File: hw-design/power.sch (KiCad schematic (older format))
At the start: 15 parts, among them CN1 CONN_02X02, CN2 CONN_02X02

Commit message: ERC passing
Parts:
- gave numbers to parts that had none: 2
- renumbered C7 to C5, C8 to C6, RT2 to RT1, RT1 to RT2
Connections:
- wire segments 42 -> 39
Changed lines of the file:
@@
 $EndDescr
 $Comp
-L CP1 C7
+L CP1 C5
 U 1 1 548B65E4
 P 7100 2300
-F 0 "C7" V 7200 2400 50  0000 L CNN
+F 0 "C5" V 7200 2400 50  0000 L CNN
 F 1 "100uF" V 6950 2200 50  0000 L CNN
 F 2 "MOD_Footprints_Lib:CAP_RAD_5MM" H 7100 2300 60  0001 C CNN
@@
 $EndComp
 $Comp
-L C C8
+L C C6
 U 1 1 548B660A
 P 7450 2300
-F 0 "C8" V 7400 2400 40  0000 L CNN
+F 0 "C6" V 7400 2400 40  0000 L CNN
 F 1 "100nF X7R" V 7600 2150 40  0000 L CNN
 F 2 "MOD_Footprints_Lib:SM0603" H 7488 2150 30  0001 C CNN
 F 3 "~" H 7450 2300 60  0000 C CNN
 	1    7450 2300
-	1    0    0    -1
-$EndComp
-$Comp
-L PWR_FLAG #FLG06
-U 1 1 548B661E
-P 7900 1900
-F 0 "#FLG06" H 7900 1995 30  0001 C CNN
-F 1 "PWR_FLAG" H 7900 2080 30  0000 C CNN
-F 2 "" H 7900 1900 60  0000 C CNN
-F 3 "" H 7900 1900 60  0000 C CNN
-	1    7900 1900
 	1    0    0    -1
 $EndComp
@@
 $EndComp
 $Comp
-L FUSE RT1
+L FUSE RT2
 U 1 1 548B6658
 P 3550 2000
-F 0 "RT1" H 3550 2100 40  0000 C CNN
+F 0 "RT2" H 3550 2100 40  0000 C CNN
 F 1 "PTC_FUSE" H 3550 1900 40  0000 C CNN
 F 2 "MOD_Footprints_Lib:SM1210" H 3550 2000 60  0001 C CNN
@@
 $EndComp
 $Comp
-L PWR_FLAG #FLG012
+L PWR_FLAG #FLG01
 U 1 1 548B666C
 P 4350 1900
-F 0 "#FLG012" H 4350 1995 30  0001 C CNN
+F 0 "#FLG01" H 4350 1995 30  0001 C CNN
 F 1 "PWR_FLAG" H 4350 2080 30  0000 C CNN
 F 2 "" H 4350 1900 60  0000 C CNN
@@
 $EndComp
 $Comp
-L PWR_FLAG #FLG015
-U 1 1 548B66C1
-P 5900 1450
-F 0 "#FLG015" H 5900 1545 30  0001 C CNN
-F 1 "PWR_FLAG" H 5900 1630 30  0000 C CNN
-F 2 "" H 5900 1450 60  0000 C CNN
-F 3 "" H 5900 1450 60  0000 C CNN
-	1    5900 1450
-	1    0    0    -1
-$EndComp
-$Comp
-L FUSE RT2
+L FUSE RT1
 U 1 1 548B66CA
 P 3550 1650
-F 0 "RT2" H 3550 1750 40  0000 C CNN
+F 0 "RT1" H 3550 1750 40  0000 C CNN
 F 1 "PTC_FUSE" H 3550 1550 40  0000 C CNN
 F 2 "MOD_Footprints_Lib:SM2920" H 3550 1650 60  0001 C CNN
@@
 $EndComp
 $Comp
-L PWR_FLAG #FLG016
+L PWR_FLAG #FLG02
 U 1 1 54B500E8
 P 3650 2450
-F 0 "#FLG016" H 3650 2545 30  0001 C CNN
+F 0 "#FLG02" H 3650 2545 30  0001 C CNN
 F 1 "PWR_FLAG" H 3650 2630 30  0000 C CNN
 F 2 "" H 3650 2450 60  0000 C CNN
@@
 $EndComp
 $Comp
-L PWR_FLAG #FLG018
+L PWR_FLAG #FLG03
 U 1 1 54B50E4C
 P 2250 1900
-F 0 "#FLG018" H 2250 1995 30  0001 C CNN
+F 0 "#FLG03" H 2250 1995 30  0001 C CNN
 F 1 "PWR_FLAG" H 2250 2080 30  0000 C CNN
 F 2 "" H 2250 1900 60  0000 C CNN
@@
 $EndComp
 $Comp
-L AP1117E50 U?
+L AP1117E50 U1
 U 1 1 54E78C99
 P 4900 2000
-F 0 "U?" H 5000 1750 50  0000 C CNN
+F 0 "U1" H 5000 1750 50  0000 C CNN
 F 1 "AP1117E50" H 4900 2250 50  0000 C CNN
 F 2 "" H 4900 2000 60  0000 C CNN
@@
 	7100 2600 7100 2500
 Wire Wire Line
-	6900 2000 7900 2000
-Wire Wire Line
 	7100 2000 7100 2100
 Wire Wire Line
@@
 Connection ~ 7450 2000
 Wire Wire Line
-	7700 1850 7700 2000
-Wire Wire Line
-	7900 2000 7900 1900
-Connection ~ 7700 2000
+	7700 2000 7700 1850
 Wire Wire Line
 	5900 2500 5900 2600
@@
 Connection ~ 5900 2000
 Wire Wire Line
-	5550 1400 5550 2100
+	5550 1800 5550 2100
 Wire Wire Line
 	2250 2000 2650 2000
-Wire Wire Line
-	5550 1500 5900 1500
-Connection ~ 5550 1500
 Wire Wire Line
 	3900 1650 3900 2000
@@
 Connection ~ 2750 3650
 $Comp
-L AP1117E33 U?
+L AP1117E33 U2
 U 1 1 54E7BA36
 P 6600 2000
-F 0 "U?" H 6700 1750 50  0000 C CNN
+F 0 "U2" H 6700 1750 50  0000 C CNN
 F 1 "AP1117E33" H 6600 2250 50  0000 C CNN
 F 2 "" H 6600 2000 60  0000 C CNN
@@
 $EndComp
 $Comp
-L VDD #PWR?
+L VDD #PWR04
 U 1 1 54E7D8DE
 P 2550 1900
-F 0 "#PWR?" H 2550 1750 60  0001 C CNN
+F 0 "#PWR04" H 2550 1750 60  0001 C CNN
 F 1 "VDD" H 2550 2050 60  0000 C CNN
 F 2 "" H 2550 1900 60  0000 C CNN
@@
 	2550 1900 2550 2000
 $Comp
-L GNDD #PWR?
+L GNDD #PWR05
 U 1 1 54E7EDE1
 P 3650 2600
-F 0 "#PWR?" H 3650 2350 60  0001 C CNN
+F 0 "#PWR05" H 3650 2350 60  0001 C CNN
 F 1 "GNDD" H 3650 2450 60  0000 C CNN
 F 2 "" H 3650 2600 60  0000 C CNN
@@
 $EndComp
 $Comp
-L GNDD #PWR?
+L GNDD #PWR06
 U 1 1 54E7EE6C
 P 4050 2600
-F 0 "#PWR?" H 4050 2350 60  0001 C CNN
+F 0 "#PWR06" H 4050 2350 60  0001 C CNN
 F 1 "GNDD" H 4050 2450 60  0000 C CNN
 F 2 "" H 4050 2600 60  0000 C CNN
@@
 $EndComp
 $Comp
-L GNDD #PWR?
+L GNDD #PWR07
 U 1 1 54E7EE80
 P 4350 2600
-F 0 "#PWR?" H 4350 2350 60  0001 C CNN
+F 0 "#PWR07" H 4350 2350 60  0001 C CNN
 F 1 "GNDD" H 4350 2450 60  0000 C CNN
 F 2 "" H 4350 2600 60  0000 C CNN
@@
 $EndComp
 $Comp
-L GNDD #PWR?
+L GNDD #PWR08
 U 1 1 54E7F5B7
 P 1500 3750
-F 0 "#PWR?" H 1500 3500 60  0001 C CNN
+F 0 "#PWR08" H 1500 3500 60  0001 C CNN
 F 1 "GNDD" H 1500 3600 60  0000 C CNN
 F 2 "" H 1500 3750 60  0000 C CNN
@@
 $EndComp
 $Comp
-L GNDD #PWR?
+L GNDD #PWR09
 U 1 1 54E7F5CB
 P 2400 3750
-F 0 "#PWR?" H 2400 3500 60  0001 C CNN
+F 0 "#PWR09" H 2400 3500 60  0001 C CNN
 F 1 "GNDD" H 2400 3600 60  0000 C CNN
 F 2 "" H 2400 3750 60  0000 C CNN
@@
 $EndComp
 $Comp
-L GNDD #PWR?
+L GNDD #PWR010
 U 1 1 54E7F5DF
 P 2750 3750
-F 0 "#PWR?" H 2750 3500 60  0001 C CNN
+F 0 "#PWR010" H 2750 3500 60  0001 C CNN
 F 1 "GNDD" H 2750 3600 60  0000 C CNN
 F 2 "" H 2750 3750 60  0000 C CNN
@@
 $EndComp
 $Comp
-L GNDD #PWR?
+L GNDD #PWR011
 U 1 1 54E7F5F3
 P 3650 3750
-F 0 "#PWR?" H 3650 3500 60  0001 C CNN
+F 0 "#PWR011" H 3650 3500 60  0001 C CNN
 F 1 "GNDD" H 3650 3600 60  0000 C CNN
 F 2 "" H 3650 3750 60  0000 C CNN
@@
 $EndComp
 $Comp
-L GNDD #PWR?
+L GNDD #PWR012
 U 1 1 54E7F9F2
 P 5550 2600
-F 0 "#PWR?" H 5550 2350 60  0001 C CNN
+F 0 "#PWR012" H 5550 2350 60  0001 C CNN
 F 1 "GNDD" H 5550 2450 60  0000 C CNN
 F 2 "" H 5550 2600 60  0000 C CNN
@@
 $EndComp
 $Comp
-L GNDD #PWR?
+L GNDD #PWR013
 U 1 1 54E7FA28
 P 5900 2600
-F 0 "#PWR?" H 5900 2350 60  0001 C CNN
+F 0 "#PWR013" H 5900 2350 60  0001 C CNN
 F 1 "GNDD" H 5900 2450 60  0000 C CNN
 F 2 "" H 5900 2600 60  0000 C CNN
@@
 $EndComp
 $Comp
-L GNDD #PWR?
+L GNDD #PWR014
 U 1 1 54E7FA3C
 P 7100 2600
-F 0 "#PWR?" H 7100 2350 60  0001 C CNN
+F 0 "#PWR014" H 7100 2350 60  0001 C CNN
 F 1 "GNDD" H 7100 2450 60  0000 C CNN
 F 2 "" H 7100 2600 60  0000 C CNN
@@
 $EndComp
 $Comp
-L GNDD #PWR?
+L GNDD #PWR015
 U 1 1 54E7FA50
 P 7450 2600
-F 0 "#PWR?" H 7450 2350 60  0001 C CNN
+F 0 "#PWR015" H 7450 2350 60  0001 C CNN
 F 1 "GNDD" H 7450 2450 60  0000 C CNN
 F 2 "" H 7450 2600 60  0000 C CNN
@@
 $EndComp
 $Comp
-L GNDD #PWR?
+L GNDD #PWR016
 U 1 1 54E80258
 P 4900 2350
-F 0 "#PWR?" H 4900 2100 60  0001 C CNN
+F 0 "#PWR016" H 4900 2100 60  0001 C CNN
 F 1 "GNDD" H 4900 2200 60  0000 C CNN
 F 2 "" H 4900 2350 60  0000 C CNN
@@
 	4900 2300 4900 2350
 $Comp
-L +5V #PWR?
+L +5V #PWR017
 U 1 1 54E80C28
-P 5550 1400
-F 0 "#PWR?" H 5550 1250 60  0001 C CNN
-F 1 "+5V" H 5550 1540 60  0000 C CNN
-F 2 "" H 5550 1400 60  0000 C CNN
-F 3 "" H 5550 1400 60  0000 C CNN
-	1    5550 1400
-	1    0    0    -1
-$EndComp
-Wire Wire Line
-	5900 1500 5900 1450
+P 5550 1800
+F 0 "#PWR017" H 5550 1650 60  0001 C CNN
+F 1 "+5V" H 5550 1940 60  0000 C CNN
+F 2 "" H 5550 1800 60  0000 C CNN
+F 3 "" H 5550 1800 60  0000 C CNN
+	1    5550 1800
+	1    0    0    -1
+$EndComp
 Wire Wire Line
 	3200 1650 3300 1650
@@
 	3800 1650 3900 1650
 $Comp
-L +3.3VP #PWR?
+L +3.3VP #PWR018
 U 1 1 54E84DA1
 P 7700 1850
-F 0 "#PWR?" H 7750 1880 20  0001 C CNN
+F 0 "#PWR018" H 7750 1880 20  0001 C CNN
 F 1 "+3.3VP" H 7700 1940 30  0000 C CNN
 F 2 "" H 7700 1850 60  0000 C CNN
@@
 	5200 2000 6300 2000
 $Comp
-L GNDD #PWR?
+L GNDD #PWR019
 U 1 1 54E876DB
 P 6600 2350
-F 0 "#PWR?" H 6600 2100 60  0001 C CNN
+F 0 "#PWR019" H 6600 2100 60  0001 C CNN
 F 1 "GNDD" H 6600 2200 60  0000 C CNN
 F 2 "" H 6600 2350 60  0000 C CNN
@@
 	6600 2300 6600 2350
 $Comp
-L +9V #PWR?
+L +9V #PWR020
 U 1 1 54E893A4
 P 4050 1850
-F 0 "#PWR?" H 4050 1700 60  0001 C CNN
+F 0 "#PWR020" H 4050 1700 60  0001 C CNN
 F 1 "+9V" H 4050 1990 60  0000 C CNN
 F 2 "" H 4050 1850 60  0000 C CNN
@@
 $EndComp
 Wire Wire Line
-	4600 2000 3800 2000
+	3800 2000 4600 2000
+Wire Wire Line
+	6900 2000 7700 2000
 $EndSCHEMATC

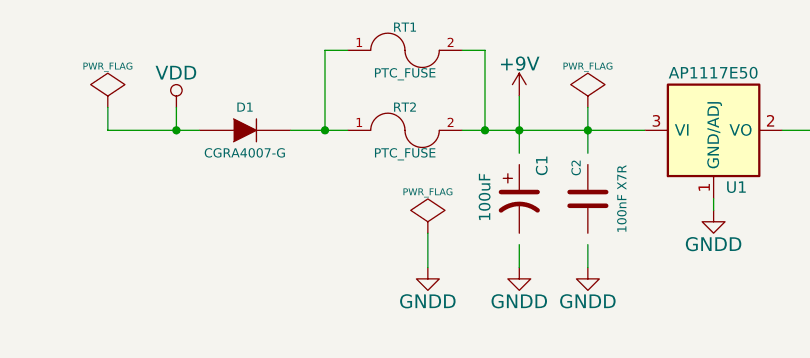
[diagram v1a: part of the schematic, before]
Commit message: removing one of the fuses
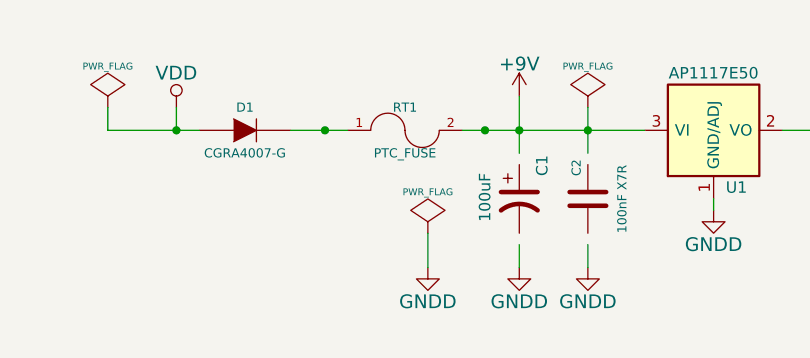
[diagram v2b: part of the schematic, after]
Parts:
- removed RT1: PTC_FUSE, MOD_Footprints_Lib:SM2920, symbol FUSE
- renumbered RT2 to RT1
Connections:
- wire segments 39 -> 35
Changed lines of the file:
@@
 $EndComp
 $Comp
-L FUSE RT2
+L FUSE RT1
 U 1 1 548B6658
 P 3550 2000
-F 0 "RT2" H 3550 2100 40  0000 C CNN
+F 0 "RT1" H 3550 2100 40  0000 C CNN
 F 1 "PTC_FUSE" H 3550 1900 40  0000 C CNN
 F 2 "MOD_Footprints_Lib:SM1210" H 3550 2000 60  0001 C CNN
@@
 $EndComp
 $Comp
-L FUSE RT1
-U 1 1 548B66CA
-P 3550 1650
-F 0 "RT1" H 3550 1750 40  0000 C CNN
-F 1 "PTC_FUSE" H 3550 1550 40  0000 C CNN
-F 2 "MOD_Footprints_Lib:SM2920" H 3550 1650 60  0001 C CNN
-F 3 "~" H 3550 1650 60  0000 C CNN
-	1    3550 1650
-	1    0    0    -1
-$EndComp
-$Comp
 L PWR_FLAG #FLG02
 U 1 1 54B500E8
@@
 Wire Wire Line
 	2250 2000 2650 2000
-Wire Wire Line
-	3900 1650 3900 2000
 Connection ~ 3900 2000
-Wire Wire Line
-	3200 1650 3200 2000
 Connection ~ 3200 2000
 Wire Wire Line
@@
 	1    0    0    -1
 $EndComp
-Wire Wire Line
-	3200 1650 3300 1650
-Wire Wire Line
-	3800 1650 3900 1650
 $Comp
 L +3.3VP #PWR018

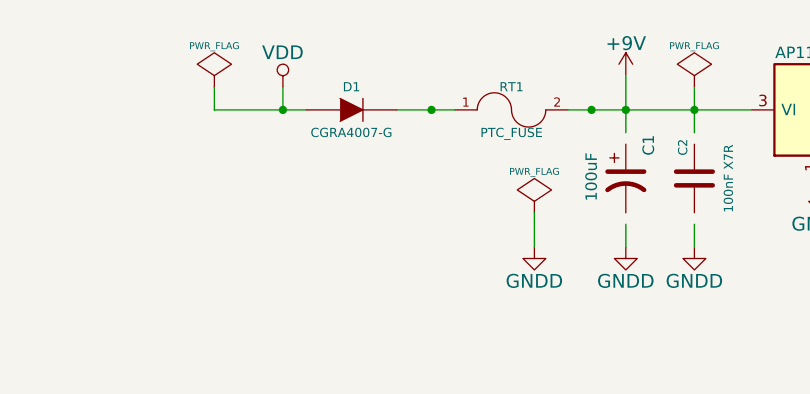
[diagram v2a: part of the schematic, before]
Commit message: wip: footprint association using default kicad libraries
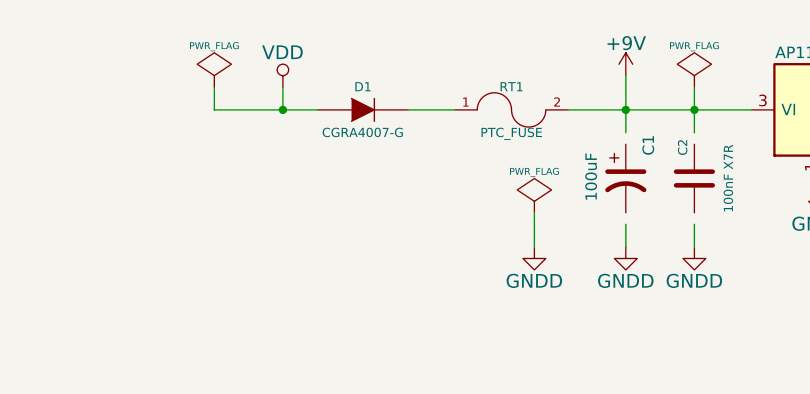
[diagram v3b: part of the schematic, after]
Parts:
- C1, C3, C5: footprint MOD_Footprints_Lib:CAP_RAD_5MM -> Capacitors_ThroughHole:Capacitor5x6RM2.5
- C2, C4, C6: footprint MOD_Footprints_Lib:SM0603 -> Capacitors_SMD:C_0603
- CN1, CN2: footprint (none) -> MOD_Footprints:CONN_PANNEL
- D1: footprint MOD_Footprints_Lib:DO-214AC(SMA) -> Diodes_SMD:Diode-SMA_Standard
- RT1: footprint MOD_Footprints_Lib:SM1210 -> Resistors_SMD:R_1210
- TP1, TP2: footprint (none) -> Pin_Headers:Pin_Header_Straight_1x01
- U1, U2: footprint (none) -> SMD_Packages:SOT-223
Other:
- moved on the sheet: D1
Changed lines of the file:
@@
 F 0 "C5" V 7200 2400 50  0000 L CNN
 F 1 "100uF" V 6950 2200 50  0000 L CNN
-F 2 "MOD_Footprints_Lib:CAP_RAD_5MM" H 7100 2300 60  0001 C CNN
+F 2 "Capacitors_ThroughHole:Capacitor5x6RM2.5" H 7100 2300 60  0001 C CNN
 F 3 "~" H 7100 2300 60  0000 C CNN
 	1    7100 2300
@@
 F 0 "C3" V 5650 2400 50  0000 L CNN
 F 1 "100uF" V 5400 2200 50  0000 L CNN
-F 2 "MOD_Footprints_Lib:CAP_RAD_5MM" H 5550 2300 60  0001 C CNN
+F 2 "Capacitors_ThroughHole:Capacitor5x6RM2.5" H 5550 2300 60  0001 C CNN
 F 3 "~" H 5550 2300 60  0000 C CNN
 	1    5550 2300
@@
 F 0 "C6" V 7400 2400 40  0000 L CNN
 F 1 "100nF X7R" V 7600 2150 40  0000 L CNN
-F 2 "MOD_Footprints_Lib:SM0603" H 7488 2150 30  0001 C CNN
+F 2 "Capacitors_SMD:C_0603" H 7488 2150 30  0001 C CNN
 F 3 "~" H 7450 2300 60  0000 C CNN
 	1    7450 2300
@@
 F 0 "C4" V 5850 2400 40  0000 L CNN
 F 1 "100nF X7R" V 6050 2150 40  0000 L CNN
-F 2 "MOD_Footprints_Lib:SM0603" H 5938 2150 30  0001 C CNN
+F 2 "Capacitors_SMD:C_0603" H 5938 2150 30  0001 C CNN
 F 3 "~" H 5900 2300 60  0000 C CNN
 	1    5900 2300
@@
 F 0 "C1" V 4150 2400 50  0000 L CNN
 F 1 "100uF" V 3900 2200 50  0000 L CNN
-F 2 "MOD_Footprints_Lib:CAP_RAD_5MM" H 4050 2300 60  0001 C CNN
+F 2 "Capacitors_ThroughHole:Capacitor5x6RM2.5" H 4050 2300 60  0001 C CNN
 F 3 "~" H 4050 2300 60  0000 C CNN
 	1    4050 2300
@@
 L DIODE D1
 U 1 1 548B6651
-P 2850 2000
-F 0 "D1" H 2850 2100 40  0000 C CNN
-F 1 "CGRA4007-G" H 2850 1900 40  0000 C CNN
-F 2 "MOD_Footprints_Lib:DO-214AC(SMA)" H 2850 2000 60  0001 C CNN
-F 3 "~" H 2850 2000 60  0000 C CNN
-	1    2850 2000
+P 2900 2000
+F 0 "D1" H 2900 2100 40  0000 C CNN
+F 1 "CGRA4007-G" H 2900 1900 40  0000 C CNN
+F 2 "Diodes_SMD:Diode-SMA_Standard" H 2900 2000 60  0001 C CNN
+F 3 "~" H 2900 2000 60  0000 C CNN
+	1    2900 2000
 	1    0    0    -1
 $EndComp
@@
 F 0 "RT1" H 3550 2100 40  0000 C CNN
 F 1 "PTC_FUSE" H 3550 1900 40  0000 C CNN
-F 2 "MOD_Footprints_Lib:SM1210" H 3550 2000 60  0001 C CNN
+F 2 "Resistors_SMD:R_1210" H 3550 2000 60  0001 C CNN
 F 3 "~" H 3550 2000 60  0000 C CNN
 	1    3550 2000
@@
 F 0 "C2" V 4300 2400 40  0000 L CNN
 F 1 "100nF X7R" V 4500 2150 40  0000 L CNN
-F 2 "MOD_Footprints_Lib:SM0603" H 4388 2150 30  0001 C CNN
+F 2 "Capacitors_SMD:C_0603" H 4388 2150 30  0001 C CNN
 F 3 "~" H 4350 2300 60  0000 C CNN
 	1    4350 2300
@@
 F 0 "U1" H 5000 1750 50  0000 C CNN
 F 1 "AP1117E50" H 4900 2250 50  0000 C CNN
-F 2 "" H 4900 2000 60  0000 C CNN
+F 2 "SMD_Packages:SOT-223" H 4900 2000 60  0001 C CNN
 F 3 "" H 4900 2000 60  0000 C CNN
 	1    4900 2000
@@
 Connection ~ 4350 2000
 Wire Wire Line
-	3050 2000 3300 2000
+	3100 2000 3300 2000
 Wire Wire Line
 	5900 1900 5900 2100
@@
 	5550 1800 5550 2100
 Wire Wire Line
-	2250 2000 2650 2000
-Connection ~ 3900 2000
-Connection ~ 3200 2000
+	2250 2000 2700 2000
 Wire Wire Line
 	3650 2450 3650 2600
@@
 F 0 "U2" H 6700 1750 50  0000 C CNN
 F 1 "AP1117E33" H 6600 2250 50  0000 C CNN
-F 2 "" H 6600 2000 60  0000 C CNN
+F 2 "SMD_Packages:SOT-223" H 6600 2000 60  0001 C CNN
 F 3 "" H 6600 2000 60  0000 C CNN
 	1    6600 2000
@@
 F 0 "CN1" H 1950 3750 50  0000 C CNN
 F 1 "CONN_02X02" H 1950 3450 50  0000 C CNN
-F 2 "" H 1950 2400 60  0000 C CNN
+F 2 "MOD_Footprints:CONN_PANNEL" H 1950 2400 60  0001 C CNN
 F 3 "" H 1950 2400 60  0000 C CNN
 	1    1950 3600
@@
 F 0 "CN2" H 3200 3750 50  0000 C CNN
 F 1 "CONN_02X02" H 3200 3450 50  0000 C CNN
-F 2 "" H 3200 2400 60  0000 C CNN
+F 2 "MOD_Footprints:CONN_PANNEL" H 3200 2400 60  0001 C CNN
 F 3 "" H 3200 2400 60  0000 C CNN
 	1    3200 3600
@@
 F 0 "TP1" H 5900 1800 50  0000 C CNN
 F 1 "~" V 6000 1700 50  0000 C CNN
-F 2 "" H 5900 1700 60  0000 C CNN
+F 2 "Pin_Headers:Pin_Header_Straight_1x01" H 5900 1700 60  0001 C CNN
 F 3 "" H 5900 1700 60  0000 C CNN
 	1    5900 1700
@@
 F 0 "TP2" H 7450 1800 50  0000 C CNN
 F 1 "~" V 7550 1700 50  0000 C CNN
-F 2 "" H 7450 1700 60  0000 C CNN
+F 2 "Pin_Headers:Pin_Header_Straight_1x01" H 7450 1700 60  0001 C CNN
 F 3 "" H 7450 1700 60  0000 C CNN
 	1    7450 1700
